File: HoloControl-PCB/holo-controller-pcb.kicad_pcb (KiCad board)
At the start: 2 copper layers, 58 parts, among them Q1 2N3904, Q2 2N3904, Q3 2N3904, Q4 2N3904, SW1 B1407 Slide Switch, SW1 PinHeader_1x04_P2.54mm_Vertic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, SW2 PBS-12B Push-Button Switch, SW2-3 PinHeader_1x04_P2.54mm_Vertic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, SW3 PBS-11B Push-Button Switch, U1 Pico

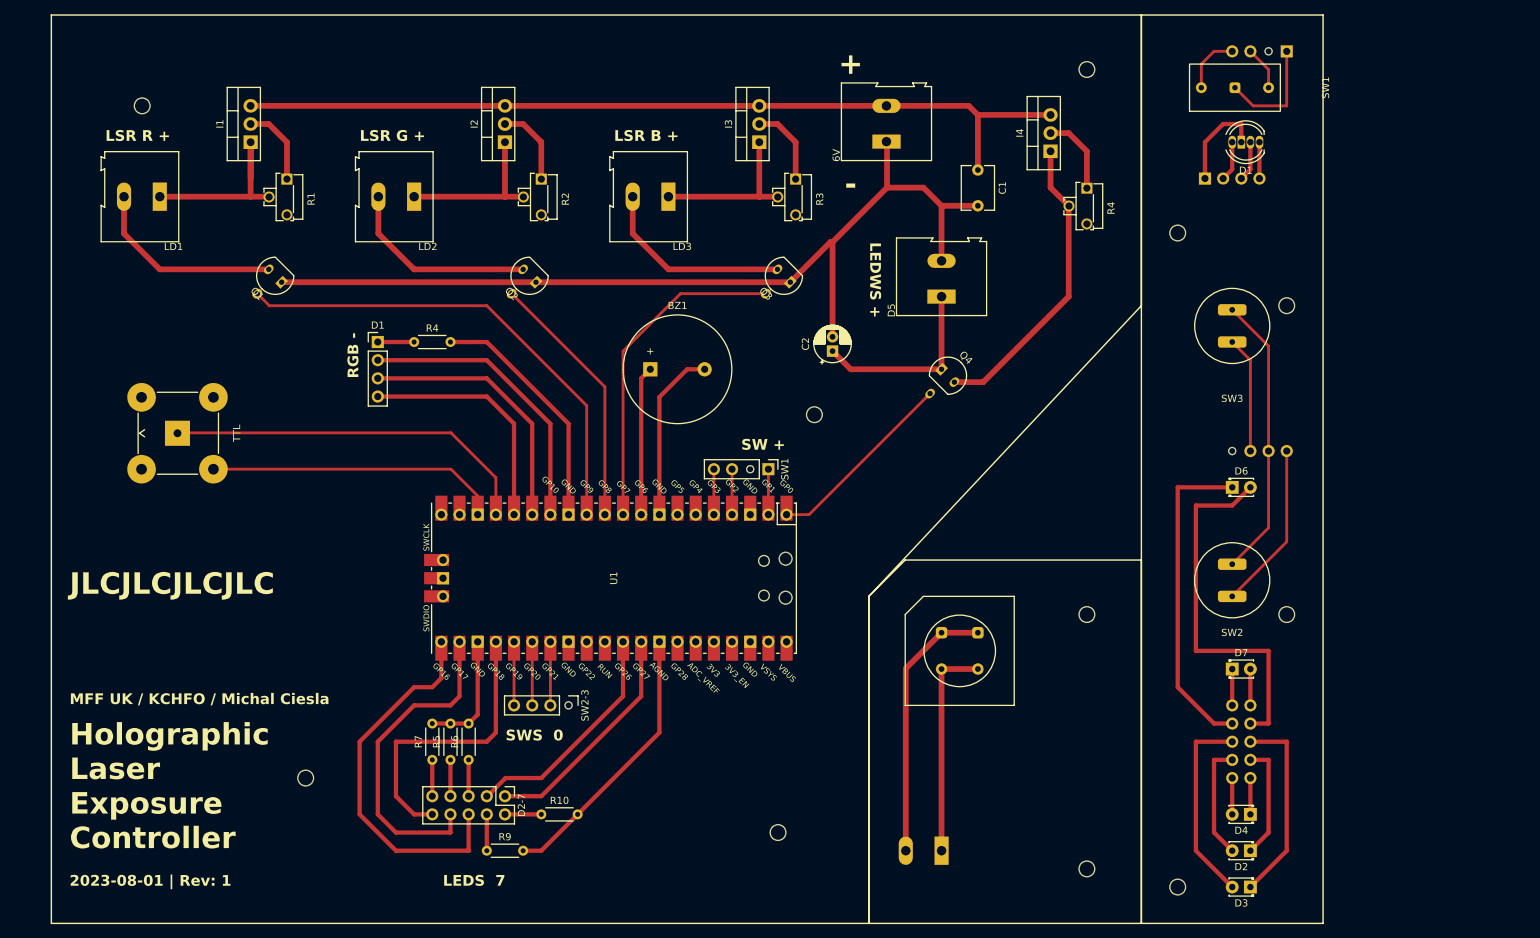
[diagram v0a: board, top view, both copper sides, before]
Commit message: Update board - Includes a change to pinout of white LEDs (swapped)
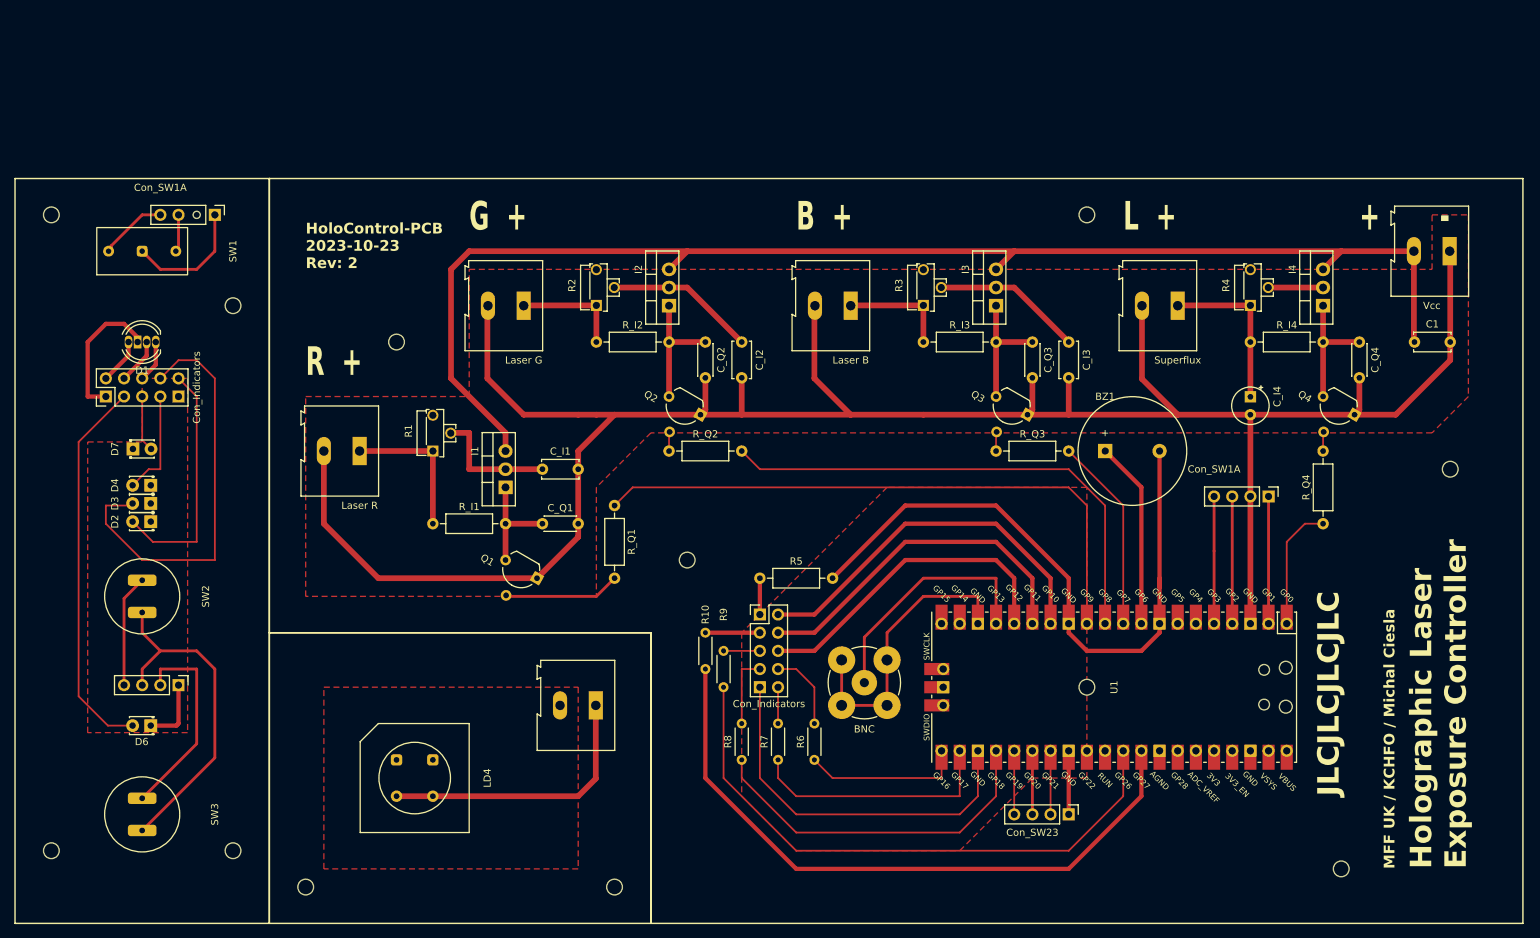
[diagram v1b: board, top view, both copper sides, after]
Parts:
- removed 6V, D5 (x2): KLS KLS2-305V-5.00-02P-3-SC, TerminalBlock:TerminalBlock_Altech_AK300-2_P5.00mm
- removed C2: HITANO CE HIT-EHR 5x11 RM2, Capacitor_THT:CP_Radial_D5.0mm_P2.00mm
- removed the D1 at (96.4, 71.1)
- removed the D1 at (219.7, 43.2)
- removed the D1 at (212.1, 48.3)
- removed D2-7 (x2): PinHeader_2x05_P2.54mm_Vertical, Connector_PinHeader_2.54mm:PinHeader_2x05_P2.54mm_Vertical
- removed the R4 at (195.6, 49.6)
- removed the R4 at (101.5, 71.1)
- removed the REF** at (208.3, 55.9)
- removed the REF** at (195.6, 33.0)
- removed the REF** at (86.4, 132.1)
- removed the REF** at (63.5, 38.1)
- removed the REF** at (223.5, 66.0)
- removed the REF** at (223.5, 109.2)
- removed the REF** at (157.5, 81.3)
- removed the REF** at (177.8, 114.3)
- removed the REF** at (195.6, 109.2)
- removed the REF** at (195.6, 144.8)
- removed the REF** at (152.4, 139.7)
- removed the REF** at (208.3, 147.3)
- removed the SW1 at (151.1, 88.9)
- removed the SW1 at (216.3, 35.6)
- removed the SW1 at (223.5, 30.5)
- removed the SW2 at (215.9, 104.4)
- removed SW2-3 (x2): PinHeader_1x04_P2.54mm_Vertical, Connector_PinHeader_2.54mm:PinHeader_1x04_P2.54mm_Vertical
- removed TTL: GOLDEN LOCH 900D-6452R2-50D, Connector_Coaxial:BNC_TEConnectivity_1478035_Horizontal
- added -9V: TerminalBlock_Altech_AK300-2_P5.00mm, TerminalBlock:TerminalBlock_Altech_AK300-2_P5.00mm, F.Cu at (246.3, 58.4)
- added C_I1: 100n, Capacitor_THT:C_Disc_D5.0mm_W2.5mm_P5.00mm, F.Cu at (119.5, 88.9)
- added C_I2: 100n, Capacitor_THT:C_Disc_D5.0mm_W2.5mm_P5.00mm, F.Cu at (147.3, 71.1)
- added C_I3: 100n, Capacitor_THT:C_Disc_D5.0mm_W2.5mm_P5.00mm, F.Cu at (193.0, 71.1)
- added C_I4: 220u, Capacitor_THT:CP_Radial_Tantal_D5.0mm_P2.50mm, F.Cu at (218.4, 78.8)
- added C_Q1: 100n, Capacitor_THT:C_Disc_D4.3mm_W1.9mm_P5.00mm, F.Cu at (119.5, 96.5)
- added C_Q2: 100n, Capacitor_THT:C_Disc_D4.3mm_W1.9mm_P5.00mm, F.Cu at (142.2, 71.1)
- added C_Q3: 100n, Capacitor_THT:C_Disc_D4.3mm_W1.9mm_P5.00mm, F.Cu at (188.0, 71.1)
- added C_Q4: 100n, Capacitor_THT:C_Disc_D4.3mm_W1.9mm_P5.00mm, F.Cu at (233.7, 71.1)
- added D1: LED_D5.0mm-4_RGB, LED_THT:LED_D5.0mm-4_RGB, F.Cu at (65.4, 71.1)
- added D1: Con_Indicators, Connector_PinHeader_2.54mm:PinHeader_2x05_P2.54mm_Vertical, F.Cu at (149.9, 109.2)
- added D1: Con_Indicators, Connector_PinHeader_2.54mm:PinHeader_2x05_P2.54mm_Vertical, F.Cu at (58.4, 78.7)
- added LD4: OSW47LZ281P, LED_THT:OSW47LZ281P, F.Cu at (101.6, 132.1)
- added LD4: TerminalBlock_Altech_AK300-2_P5.00mm, TerminalBlock:TerminalBlock_Altech_AK300-2_P5.00mm, F.Cu at (126.9, 121.9)
- added LD4: TerminalBlock_Altech_AK300-2_P5.00mm, TerminalBlock:TerminalBlock_Altech_AK300-2_P5.00mm, F.Cu at (208.3, 66.0)
- added R4: 50R, Potentiometer_THT:Potentiometer_Runtron_RM-063_Horizontal, F.Cu at (218.4, 66.0)
- added R8: 10k, Resistor_THT:R_Axial_DIN0204_L3.6mm_D1.6mm_P5.08mm_Horizontal, F.Cu at (147.3, 129.5)
- added REF**: MountingHole_2.2mm_M2, MountingHole:MountingHole_2.2mm_M2, F.Cu at (129.5, 147.3)
- added REF**: MountingHole_2.2mm_M2, MountingHole:MountingHole_2.2mm_M2, F.Cu at (246.4, 88.9)
- added REF**: MountingHole_2.2mm_M2, MountingHole:MountingHole_2.2mm_M2, F.Cu at (231.1, 144.8)
- added REF**: MountingHole_2.2mm_M2, MountingHole:MountingHole_2.2mm_M2, F.Cu at (195.6, 53.3)
- added REF**: MountingHole_2.2mm_M2, MountingHole:MountingHole_2.2mm_M2, F.Cu at (76.2, 66.0)
- added REF**: MountingHole_2.2mm_M2, MountingHole:MountingHole_2.2mm_M2, F.Cu at (139.7, 101.6)
- added REF**: MountingHole_2.2mm_M2, MountingHole:MountingHole_2.2mm_M2, F.Cu at (76.2, 142.2)
- added REF**: MountingHole_2.2mm_M2, MountingHole:MountingHole_2.2mm_M2, F.Cu at (195.6, 119.4)
- added REF**: MountingHole_2.2mm_M2, MountingHole:MountingHole_2.2mm_M2, F.Cu at (50.8, 53.3)
- added REF**: MountingHole_2.2mm_M2, MountingHole:MountingHole_2.2mm_M2, F.Cu at (86.4, 147.3)
- added REF**: MountingHole_2.2mm_M2, MountingHole:MountingHole_2.2mm_M2, F.Cu at (99.1, 71.1)
- added REF**: BNC, Connector_Coaxial:BNC_TEConnectivity_1478204_Vertical, F.Cu at (164.5, 118.7)
- added REF**: MountingHole_2.2mm_M2, MountingHole:MountingHole_2.2mm_M2, F.Cu at (50.8, 142.2)
- added R_I1: 1k, Resistor_THT:R_Axial_DIN0207_L6.3mm_D2.5mm_P10.16mm_Horizontal, F.Cu at (104.1, 96.5)
- added R_I2: 1k, Resistor_THT:R_Axial_DIN0207_L6.3mm_D2.5mm_P10.16mm_Horizontal, F.Cu at (127.0, 71.1)
- added R_I3: 1k, Resistor_THT:R_Axial_DIN0207_L6.3mm_D2.5mm_P10.16mm_Horizontal, F.Cu at (172.7, 71.1)
- added R_I4: 1k, Resistor_THT:R_Axial_DIN0207_L6.3mm_D2.5mm_P10.16mm_Horizontal, F.Cu at (218.4, 71.1)
- added R_Q1: 4k7, Resistor_THT:R_Axial_DIN0207_L6.3mm_D2.5mm_P10.16mm_Horizontal, F.Cu at (129.5, 94.0)
- added R_Q2: 4k7, Resistor_THT:R_Axial_DIN0207_L6.3mm_D2.5mm_P10.16mm_Horizontal, F.Cu at (137.2, 86.4)
- added R_Q3: 4k7, Resistor_THT:R_Axial_DIN0207_L6.3mm_D2.5mm_P10.16mm_Horizontal, F.Cu at (182.9, 86.4)
- added R_Q4: 4k7, Resistor_THT:R_Axial_DIN0207_L6.3mm_D2.5mm_P10.16mm_Horizontal, F.Cu at (228.6, 96.5)
- added SW1: B1407 Slide Switch, Button_Switch_THT:B1407 Slide Switch, F.Cu at (63.5, 58.4)
- added SW1A: Con_SW1A, Connector_PinHeader_2.54mm:PinHeader_1x04_P2.54mm_Vertical, F.Cu at (73.7, 53.3)
- added SW1A: Con_SW1A, Connector_PinHeader_2.54mm:PinHeader_1x04_P2.54mm_Vertical, F.Cu at (221.0, 92.7)
- added SW2: Con_SW23, Connector_PinHeader_2.54mm:PinHeader_1x04_P2.54mm_Vertical, F.Cu at (68.6, 119.1)
- added SW2: Con_SW23, Connector_PinHeader_2.54mm:PinHeader_1x04_P2.54mm_Vertical, F.Cu at (193.0, 137.2)
- added SW2: PBS-12B Push-Button Switch, Button_Switch_THT:PBS-12B Push-Button Switch, F.Cu at (63.5, 106.7)
- BZ1: value KINGSTATE KPEG242 -> Buzzer
- C1: value HITANO CK Z5U RM5,00 -> 1u; footprint Capacitor_THT:C_Disc_D6.0mm_W4.4mm_P5.00mm -> Capacitor_THT:C_Disc_D5.0mm_W2.5mm_P5.00mm
- I1, I2, I3: value LM317T-DG -> LM317T
- I4: value LM317_TO-220 -> LM317T
- LD1, LD2, LD3: value KLS KLS2-305V-5.00-02P-3-SC -> TerminalBlock_Altech_AK300-2_P5.00mm
- Q1, Q2, Q3, Q4: footprint Package_TO_SOT_THT:TO-92_Inline -> Package_TO_SOT_THT:TO-92_Inline_Wide
- R1, R2, R3: value 64 Y 50R CN -> 50R
- R10, R6, R9: value HITANO RM 330R 0,4W 1% 0204 -> 10k
- R5: value HITANO RM 330R 0,4W 1% 0204 -> 4k7; footprint Resistor_THT:R_Axial_DIN0204_L3.6mm_D1.6mm_P5.08mm_Horizontal -> Resistor_THT:R_Axial_DIN0207_L6.3mm_D2.5mm_P10.16mm_Horizontal
- R7: value HITANO RM 330R 0,4W 1% 0204 -> 4k7
- moved SW3 167.0 mm to (63.5, 137.2)
- moved D3 162.8 mm to (64.7, 93.7)
- moved D2 160.5 mm to (64.7, 96.2)
- moved D4 160.5 mm to (64.7, 91.2)
- moved D7 156.7 mm to (62.2, 86.1)
- moved D6 154.8 mm to (64.7, 124.8), turned to 180 degrees
- moved U1 71.6 mm to (199.4, 119.4)
- moved C1 65.6 mm to (241.4, 71.1), turned to 0 degrees
- moved BZ1 64.6 mm to (198.1, 86.4)
- moved I1 60.0 mm to (114.3, 91.4)
- moved Q4 58.1 mm to (233.0, 81.3), turned to 150 degrees
- moved Q1 54.7 mm to (118.7, 104.1), turned to 150 degrees
- moved R5 50.2 mm to (149.9, 104.1), turned to 0 degrees
- moved R7 48.3 mm to (152.4, 129.5)
- moved R6 48.3 mm to (157.5, 129.5)
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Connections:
- net BuzzerIn renamed BZ1+
- net DC-4 renamed LED-B
- net I4-Reference renamed I4-Adj
- net Q1-Logic renamed Q1
- net Q2-Logic renamed Q2
- net Q3-Logic renamed Q3
- net Q4-Logic renamed Q4
- BZ1 pad 2: BuzzerOut -> D-GND
- D2 pad 1: DC-2O -> D-GND
- D2 pad 2: DC-2 -> LED-R
- D3 pad 1: DC-3O -> D-GND
- D3 pad 2: DC-3 -> LED-G
- D4 pad 1: DC-4O -> D-GND
- D6 pad 1: DW-6O -> D-GND
- D6 pad 2: DW-6 -> LED-W
- D7 pad 1: DW-7O -> D-GND
- D7 pad 2: DW-7 -> LED-WW
- I1 pad 1: I1-Reference -> I1-Adj
- I1 pad 2: I1-Output -> I1-Vo
- I2 pad 1: I2-Reference -> I2-Adj
- I2 pad 2: I2-Output -> I2-Vo
- I3 pad 1: I3-Reference -> I3-Adj
- I3 pad 2: I3-Output -> I3-Vo
- I4 pad 2: I4-Output -> I4-Vo
- LD1 pad 1: I1-Reference -> -9V
- LD1 pad 2: Laser1 -> I1
- LD2 pad 1: I2-Reference -> -9V
- LD2 pad 2: Laser2 -> I2
- LD3 pad 1: Laser3 -> -9V
- LD3 pad 2: I3-Reference -> I3
- Q1 pad 3: Laser1 -> I1-Adj
- Q2 pad 3: Laser2 -> I2-Adj
- Q3 pad 3: Laser3 -> I3-Adj
- Q4 pad 1: Superflux -> -9V
- R1 pad 1: I1-Output -> I1
- R1 pad 2: I1-Reference -> I1-Vo
- R10 pad 1: DW-7O -> LED-W
- R10 pad 2: DW-G -> LED-W
- R2 pad 1: I2-Output -> I2
- R2 pad 2: I2-Reference -> I2-Vo
- R3 pad 1: I3-Output -> I3
- R3 pad 2: I3-Reference -> I3-Vo
- R5 pad 1: DC-2O -> D1-C
- R5 pad 2: DC-G -> D-GND
- R6 pad 1: DC-3O -> LED-G
- R6 pad 2: DC-G -> LED-G
- R7 pad 1: DC-4O -> LED-R
- R7 pad 2: DC-G -> LED-R
- R9 pad 1: DW-6O -> LED-WW
- R9 pad 2: DW-G -> LED-WW
- SW3 pad 1: SW2-3-02 -> SW-In
- SW3 pad 2: SW2-3-IN -> SW3-Out
- U1 pad 13: D1-R4 -> D-GND
- U1 pad 14: D1-RA -> D1-R
- U1 pad 15: D1-GA -> D1-G
- U1 pad 16: D1-BA -> D1-B
- U1 pad 17: VBUS -> TTL-VBUS
- U1 pad 18: GND -> TTL-GND
- U1 pad 19: unconnected-(U1-GPIO14-Pad19) -> (no net)
- U1 pad 2: SW1-IN -> SW1-In
- U1 pad 20: unconnected-(U1-GPIO15-Pad20) -> (no net)
- U1 pad 21: DC-3 -> LED-G
- U1 pad 22: DC-2 -> LED-R
- U1 pad 23: DC-G -> D-GND
- U1 pad 25: SW2-3-O1 -> SW2-Out
- U1 pad 26: SW2-3-IN -> SW-In
- U1 pad 27: SW2-3-02 -> SW3-Out
- U1 pad 28: unconnected-(U1-GND-Pad28) -> D-GND
- U1 pad 29: unconnected-(U1-GPIO22-Pad29) -> (no net)
- U1 pad 3: unconnected-(U1-GND-Pad3) -> -9V
- U1 pad 30: unconnected-(U1-RUN-Pad30) -> (no net)
- U1 pad 31: DW-6 -> LED-WW
- U1 pad 32: DW-7 -> LED-W
- U1 pad 33: DW-G -> (no net)
- U1 pad 34: unconnected-(U1-GPIO28_ADC2-Pad34) -> (no net)
- U1 pad 35: unconnected-(U1-ADC_VREF-Pad35) -> (no net)
- U1 pad 36: unconnected-(U1-3V3-Pad36) -> (no net)
- U1 pad 37: unconnected-(U1-3V3_EN-Pad37) -> (no net)
- U1 pad 38: unconnected-(U1-GND-Pad38) -> (no net)
- U1 pad 39: unconnected-(U1-VSYS-Pad39) -> (no net)
- U1 pad 4: SW1-O1 -> SW1-M
- U1 pad 40: unconnected-(U1-VBUS-Pad40) -> (no net)
- U1 pad 41: unconnected-(U1-SWCLK-Pad41) -> (no net)
- U1 pad 42: unconnected-(U1-GND-Pad42) -> (no net)
- U1 pad 43: unconnected-(U1-SWDIO-Pad43) -> (no net)
- U1 pad 5: SW1-O2 -> SW1-A
- U1 pad 6: unconnected-(U1-GPIO4-Pad6) -> (no net)
- U1 pad 7: unconnected-(U1-GPIO5-Pad7) -> (no net)
- U1 pad 8: BuzzerOut -> D-GND
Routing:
- net D-GND: track 0.00 -> 161.5 mm
- net -9V: track 169.0 -> 326.4 mm
- net LED-W: track 0.00 -> 153.4 mm
- net LED-WW: track 0.00 -> 95.2 mm
- net LED-G: track 0.00 -> 92.7 mm
- net DW-6: track 84.3 -> 0.00 mm
- net DC-3: track 80.3 -> 0.00 mm
- net LED-R: track 0.00 -> 74.5 mm
- net +9V: track 120.1 -> 187.7 mm
- net I4: track 0.00 -> 62.1 mm
- net DC-2: track 61.9 -> 0.00 mm
- net D1-R: track 0.00 -> 59.3 mm
- net Superflux: track 56.9 -> 0.00 mm
- net SW-In: track 0.00 -> 56.6 mm
- net D1-G: track 0.00 -> 55.7 mm
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- added copper zone on F.Cu, net -9V
- added copper zone on F.Cu, net D-GND
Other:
- board text added: "+ -"
- board text added: "B +"
- board text added: "G +"
- board text added: "HoloControl-PCB ${ISSUE_DATE} Rev: ${REVISION}"
- board text added: "L +"
- board text added: "MFF UK / KCHFO / Michal Ciesla"
- board text added: "R +"
- board text removed: "${COMPANY}"
- board text removed: "${ISSUE_DATE} | Rev: ${REVISION}"
- board text removed: "+"
- board text removed: "-"
- board text removed: "LEDS 7"
- board text removed: "LEDWS +"
- board text removed: "LSR B +"
- board text removed: "LSR G +"
- board text removed: "LSR R +"
- board text removed: "RGB -"
- board text removed: "SW +"
- board text removed: "SWS 0"

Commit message: Finished KiCad schematic and board
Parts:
- LD4: moved to B.Cu
- moved LD4 7.62 mm to (109.2, 132.1)
- moved LD4 4.92 mm to (122.0, 121.9), turned to 0 degrees
- moved REF** 2.54 mm to (88.9, 147.3)
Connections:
- LD4 pad 1: -9V -> I4
- LD4 pad 2: I4 -> -9V
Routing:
- net I4: track 62.1 -> 54.5 mm
